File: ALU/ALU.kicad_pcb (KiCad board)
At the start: 4 copper layers, 100 x 100 mm, 73 parts, among them IC1 SN74AHCT16245ADGGR, J1 Conn_01x06_Pin, J2 Conn_02x15_Odd_Even, J3 Conn_02x15_Odd_Even, J4 Conn_02x15_Odd_Even, J5 Conn_01x01_Pin, J6 Conn_01x01_Pin, J7 Conn_01x01_Pin, J8 Conn_01x01_Pin, U1 74AHC1G08, U10 74HCT21, U11 74AHCT1G02, U12 74AHCT1G02, U13 74AHC1G08, U14 74AHC1G08, U15 74AHCT1G02, U16 74AHCT1G02, U17 74AHC1G08, U18 SN74AHC16374DGGR, U19 74AHC1G08, U2 SN74AHC16374DGGR, U20 74AHCT1G02, U21 74AHCT1G02, U3 74AHC1G04, U4 74LS181, U5 74LS181, U6 74AHC1G08, U7 74HCT11, U8 74LS181, U9 74LS181

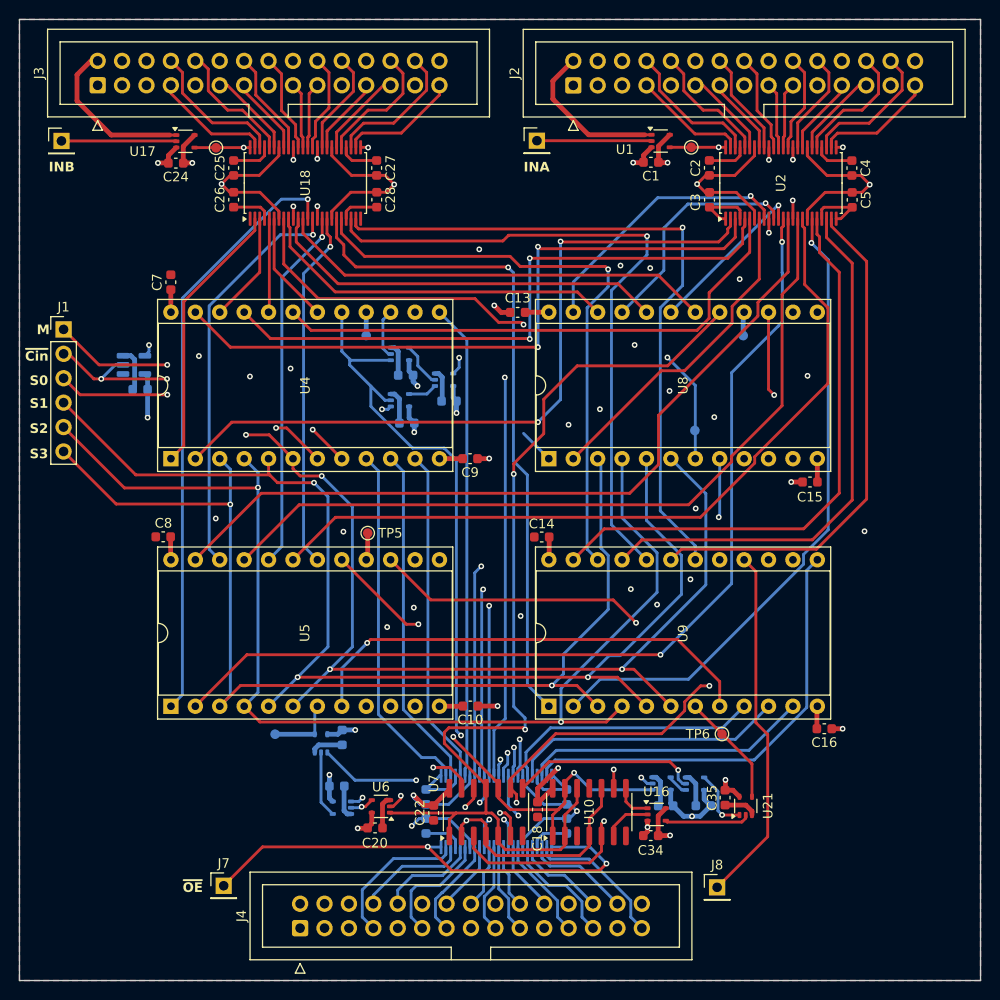
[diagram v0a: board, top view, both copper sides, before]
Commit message: Updated ALU and moved common schematics to common/ for enhanced reusability
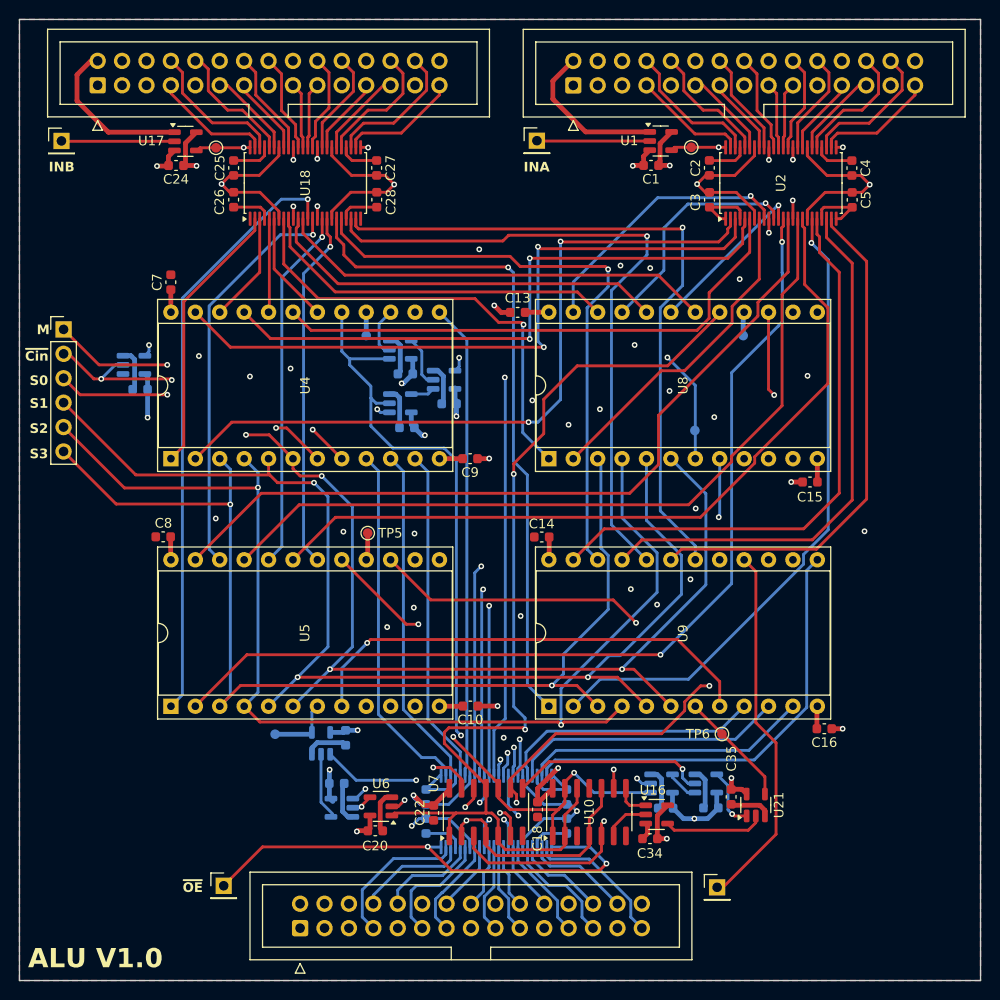
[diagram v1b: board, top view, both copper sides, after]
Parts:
- U1, U17: footprint Package_TO_SOT_SMD:SOT-353_SC-70-5 -> Package_TO_SOT_SMD:SOT-23-5
- U11, U15, U16: value 74AHCT1G02 -> 74AHC1G32DBVR; footprint Package_TO_SOT_SMD:SOT-353_SC-70-5 -> Package_TO_SOT_SMD:SOT-23-5
- U12, U20, U21: value 74AHCT1G02 -> 74AHCT1G02DBVR; footprint Package_TO_SOT_SMD:SOT-353_SC-70-5 -> Package_TO_SOT_SMD:SOT-23-5
- U13, U14, U19, U6: value 74AHC1G08 -> 74AHCT1G08DBVR; footprint Package_TO_SOT_SMD:SOT-353_SC-70-5 -> Package_TO_SOT_SMD:SOT-23-5
- moved U15 1.13 mm to (205.4, 93.5)
- moved U21 1.05 mm to (210.6, 95.7)
- moved C33 0.82 mm to (205.9, 96.0)
- moved C35 0.64 mm to (208.1, 94.9)
- moved C12 0.47 mm to (174.3, 56.5)
- moved U19 0.45 mm to (173.6, 48.4)
- moved C21 0.36 mm to (167.9, 88.7)
- moved C34 0.33 mm to (199.6, 99.2)
- moved C1 0.33 mm to (199.7, 29.2)
- moved U13 0.31 mm to (173.6, 53.9)
- moved C20 0.30 mm to (171.0, 98.4)
- moved C19 0.28 mm to (178.7, 54.0)
- moved C11 0.28 mm to (167.0, 93.5)
- moved C24 0.25 mm to (150.3, 29.2)
- moved C23 0.25 mm to (201.2, 96.1)
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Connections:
- net /alu16/carry generator/~{Cin} renamed /alu16/carry generator/Cin
- J2 pad 2: /CLK -> /bus_connector/CLK
- J3 pad 2: /CLK -> /bus_connector2/CLK
- U1 pad 1: /CLK -> /bus_connector/CLK
- U17 pad 1: /CLK -> /bus_connector2/CLK
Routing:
- net /CLK: track 33.9 -> 0.00 mm
- net /bus_connector2/CLK: track 0.00 -> 17.0 mm
- net /bus_connector/CLK: track 0.00 -> 16.4 mm
- net /INB/DOUT4: track 36.0 -> 47.4 mm
- net GND: track 139.0 -> 147.3 mm, vias 39 -> 41
- net +5V: track 171.4 -> 175.4 mm
- net Net-(U16-Pad4): track 8.87 -> 10.7 mm
- net Net-(U14-Pad4): track 2.21 -> 3.30 mm
- net /alu16/Cout: track 37.3 -> 38.4 mm
- net Net-(U19-Pad4): track 4.63 -> 5.59 mm
- net Net-(U15-Pad2): track 19.6 -> 20.6 mm
- net /INA/DOUT1: track 70.7 -> 71.6 mm
- net /alu16/carry generator/Cin: track 98.6 -> 98.0 mm
- net /S2: track 123.4 -> 124.1 mm
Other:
- board text added: "ALU V1.0"

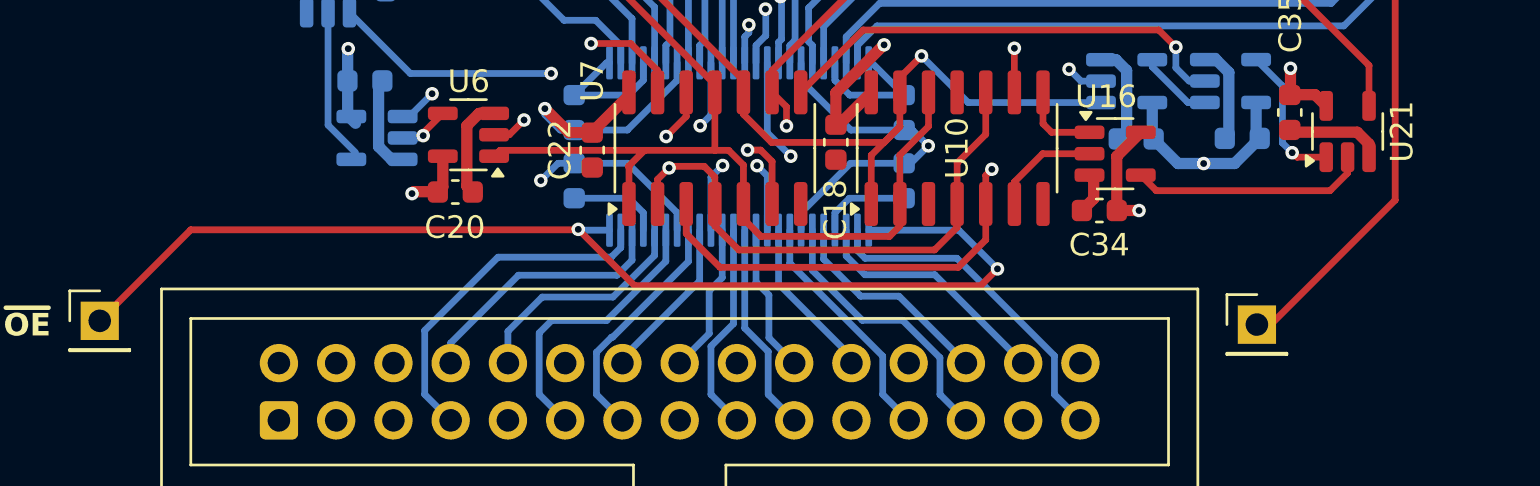
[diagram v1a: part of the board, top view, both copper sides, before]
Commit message: Fixed tri-state buffer and completed double buffer PCB
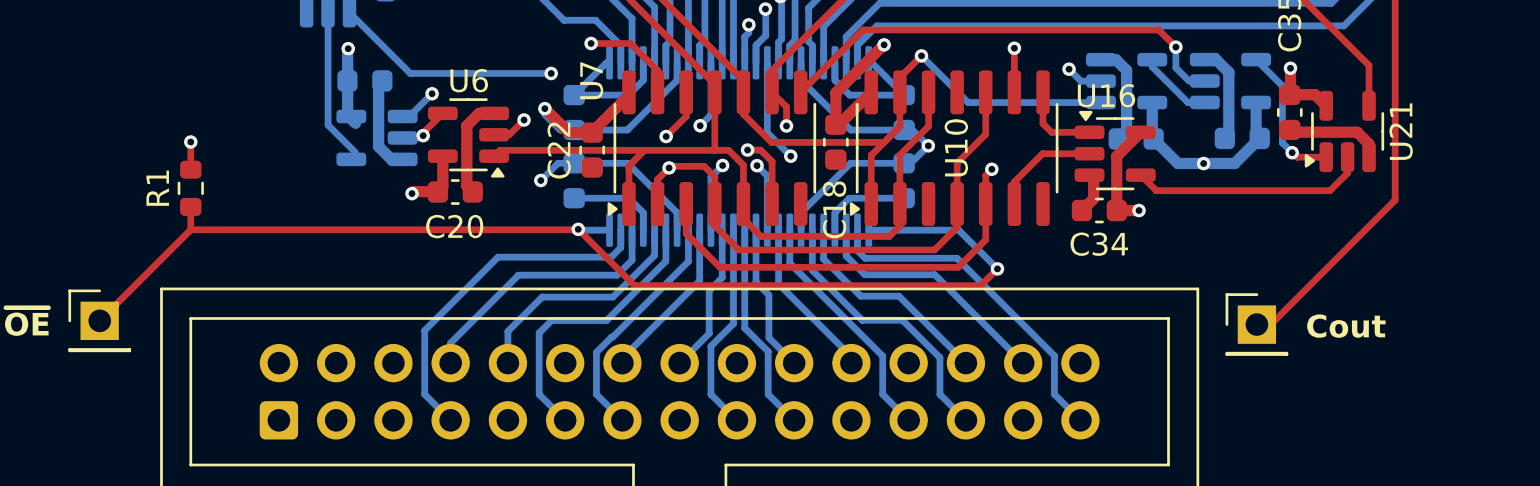
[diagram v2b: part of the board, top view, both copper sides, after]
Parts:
- added R1: 1k, Resistor_SMD:R_0603_1608Metric, F.Cu at (159.3, 98.3)
- IC1: value SN74AHCT16245ADGGR -> SN74AHCT16245DGVR
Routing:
- net +5V: track 175.4 -> 176.6 mm, vias 24 -> 25
- net /Tri-State Buf16/~{OE}: track 50.7 -> 51.7 mm
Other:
- board text added: "Cout"

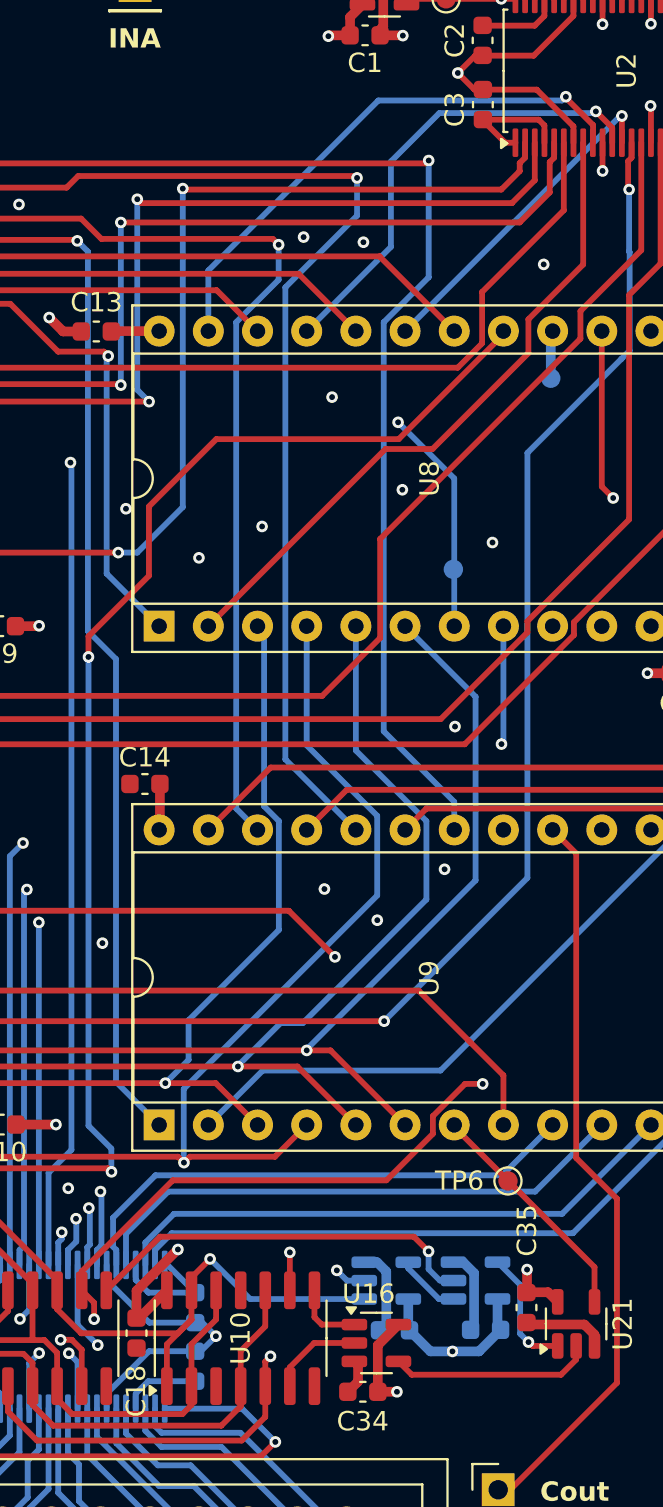
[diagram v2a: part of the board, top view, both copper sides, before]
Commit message: Fixed ERC errors
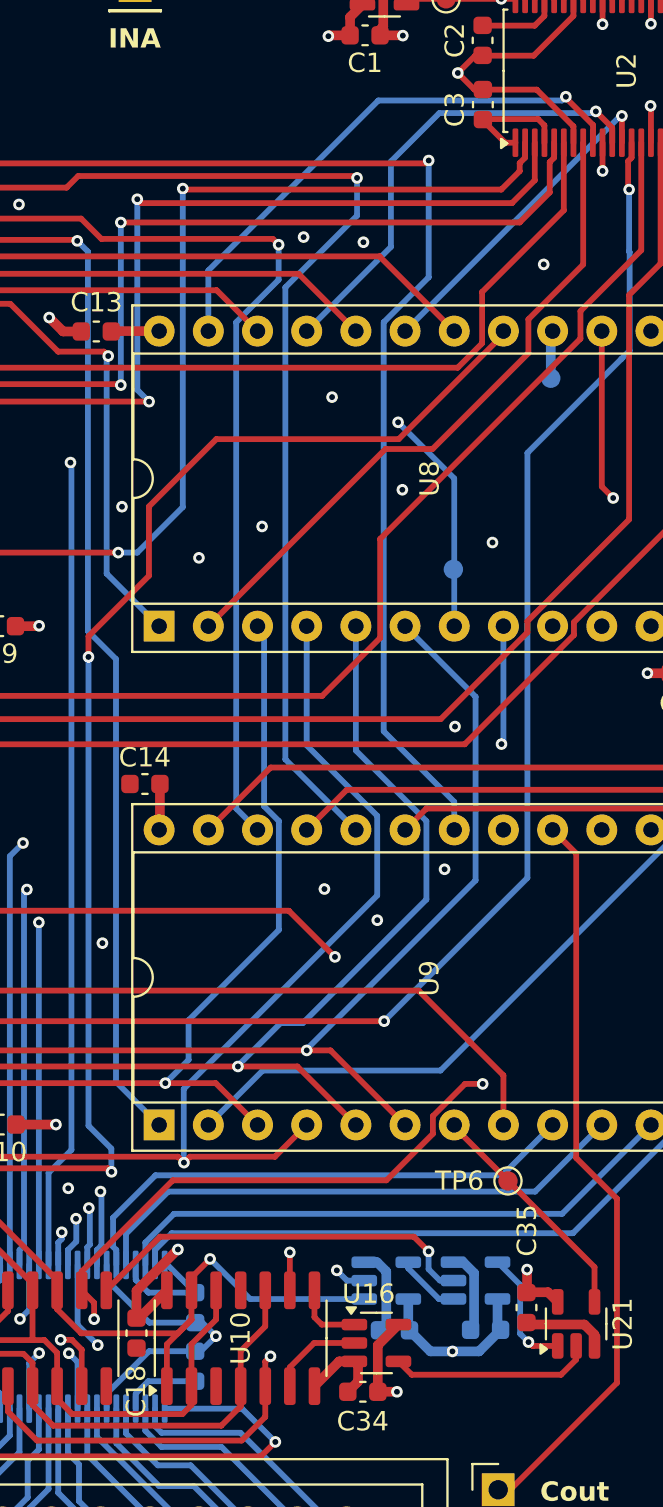
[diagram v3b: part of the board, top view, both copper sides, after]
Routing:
- net GND: track 147.3 -> 150.0 mm
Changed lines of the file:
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@@
+	)
+	(segment
+		(start 208.977 33.837)
+		(end 208.977 34.74)
+		(width 0.3)
+		(layer "F.Cu")
+		(net 1)
+	)
+	(segment
+		(start 205.734 33.51)
+		(end 208.65 33.51)
+		(width 0.3)
+		(layer "F.Cu")
+		(net 1)
 	)
 	(segment
@@
 	)
 	(segment
+		(start 208.65 33.51)
+		(end 208.977 33.837)
+		(width 0.3)
+		(layer "F.Cu")
+		(net 1)
+	)
+	(segment
 		(start 205.7641 28.685)
 		(end 208.475 28.685)
@@
 	)
 	(segment
+		(start 206.954 34.73)
+		(end 205.734 33.51)
+		(width 0.3)
+		(layer "F.Cu")
+		(net 1)
+	)
+	(segment
 		(start 162.4991 33.4509)
 		(end 162.5 33.45)
@@
 	)
 	(segment
+		(start 149.497 28.2621)
+		(end 150.1291 27.63)
+		(width 0.5)
+		(layer "F.Cu")
+		(net 1)
+	)
+	(segment
+		(start 198.38 97.67)
+		(end 197.1 98.95)
+		(width 0.5)
+		(layer "F.Cu")
+		(net 1)
+	)
+	(segment
 		(start 205.764 28.685)
 		(end 205.7641 28.685)
@@
 	)
 	(segment
-		(start 206.954 34.73)
-		(end 205.764 33.54)
-		(width 0.3)
-		(layer "F.Cu")
-		(net 1)
-	)
-	(segment
 		(start 217.02 59.7)
 		(end 217.02 62.12)
@@
 	)
 	(segment
-		(start 149.497 28.2621)
-		(end 150.1291 27.63)
-		(width 0.5)
-		(layer "F.Cu")
-		(net 1)
-	)
-	(segment
 		(start 218.9791 34.73)
 		(end 218.979 34.73)
@@
 	)
 	(segment
+		(start 199.1625 97.67)
+		(end 198.38 97.67)
+		(width 0.5)
+		(layer "F.Cu")
+		(net 1)
+	)
+	(segment
 		(start 208.977 28.1835)
 		(end 208.977 27.315)
@@
 	)
 	(segment
+		(start 171.1666 28.675)
+		(end 168.596 28.675)
+		(width 0.3)
+		(layer "F.Cu")
+		(net 1)
+	)
+	(segment
+		(start 216.97 85.51)
+		(end 217.02 85.46)
+		(width 0.5)
+		(layer "F.Cu")
+		(net 1)
+	)
+	(segment
+		(start 177.7 59.7)
+		(end 180.11 59.7)
+		(width 0.5)
+		(layer "F.Cu")
+		(net 1)
+	)
+	(segment
+		(start 217.477 34.74)
+		(end 217.477 33.768)
+		(width 0.3)
+		(layer "F.Cu")
+		(net 1)
+	)
+	(segment
+		(start 148.31 29.255)
+		(end 149.419 29.255)
+		(width 0.5)
+		(layer "F.Cu")
+		(net 1)
+	)
+	(segment
+		(start 184.12 44.48)
+		(end 183.4 43.76)
+		(width 0.5)
+		(layer "F.Cu")
+		(net 1)
+	)
+	(segment
+		(start 162.4991 27.305)
+		(end 162.4991 28.6091)
+		(width 0.3)
+		(layer "F.Cu")
+		(net 1)
+	)
+	(segment
+		(start 164.9991 34.73)
+		(end 164.9991 33.4309)
+		(width 0.3)
+		(layer "F.Cu")
+		(net 1)
+	)
+	(segment
+		(start 216.97 87.8)
+		(end 216.97 85.51)
+		(width 0.5)
+		(layer "F.Cu")
+		(net 1)
+	)
+	(segment
+		(start 199.1625 97.67)
+		(end 199.35 97.8575)
+		(width 0.5)
+		(layer "F.Cu")
+		(net 1)
+	)
+	(segment
+		(start 168.426 33.53)
+		(end 171.1766 33.53)
+		(width 0.3)
+		(layer "F.Cu")
+		(net 1)
+	)
+	(segment
+		(start 208.05 95.665)
+		(end 208.15 95.765)
+		(width 0.5)
+		(layer "F.Cu")
+		(net 1)
+	)
+	(segment
+		(start 171.167 28.675)
+		(end 171.1666 28.675)
+		(width 0.3)
+		(layer "F.Cu")
+		(net 1)
+	)
+	(segment
+		(start 167.999 28.0783)
+		(end 167.999 27.305)
+		(width 0.3)
+		(layer "F.Cu")
+		(net 1)
+	)
+	(segment
+		(start 220.654 33.54)
+		(end 219.464 34.73)
+		(width 0.3)
+		(layer "F.Cu")
+		(net 1)
+	)
+	(segment
+		(start 180.04 85.46)
+		(end 180.06 85.44)
+		(width 0.5)
+		(layer "F.Cu")
+		(net 1)
+	)
+	(segment
 		(start 207.479 34.73)
 		(end 206.954 34.73)
@@
 	)
 	(segment
-		(start 171.1666 28.675)
-		(end 168.596 28.675)
-		(width 0.3)
-		(layer "F.Cu")
-		(net 1)
-	)
-	(segment
-		(start 216.97 85.51)
-		(end 217.02 85.46)
-		(width 0.5)
-		(layer "F.Cu")
-		(net 1)
-	)
-	(segment
-		(start 208.977 33.837)
-		(end 208.977 34.74)
-		(width 0.3)
-		(layer "F.Cu")
-		(net 1)
-	)
-	(segment
-		(start 177.7 59.7)
-		(end 180.11 59.7)
-		(width 0.5)
-		(layer "F.Cu")
-		(net 1)
-	)
-	(segment
-		(start 217.477 34.74)
-		(end 217.477 33.768)
-		(width 0.3)
-		(layer "F.Cu")
-		(net 1)
-	)
-	(segment
-		(start 148.31 29.255)
-		(end 149.419 29.255)
-		(width 0.5)
-		(layer "F.Cu")
-		(net 1)
-	)
-	(segment
-		(start 184.12 44.48)
-		(end 183.4 43.76)
-		(width 0.5)
-		(layer "F.Cu")
-		(net 1)
-	)
-	(segment
-		(start 162.4991 27.305)
-		(end 162.4991 28.6091)
-		(width 0.3)
-		(layer "F.Cu")
-		(net 1)
-	)
-	(segment
-		(start 164.9991 34.73)
-		(end 164.9991 33.4309)
-		(width 0.3)
-		(layer "F.Cu")
-		(net 1)
-	)
-	(segment
-		(start 216.97 87.8)
-		(end 216.97 85.51)
-		(width 0.5)
-		(layer "F.Cu")
-		(net 1)
-	)
-	(segment
-		(start 199.1625 97.67)
-		(end 199.35 97.8575)
-		(width 0.5)
-		(layer "F.Cu")
-		(net 1)
-	)
-	(segment
-		(start 168.426 33.53)
-		(end 171.1766 33.53)
-		(width 0.3)
-		(layer "F.Cu")
-		(net 1)
-	)
-	(segment
-		(start 208.05 95.665)
-		(end 208.15 95.765)
-		(width 0.5)
-		(layer "F.Cu")
-		(net 1)
-	)
-	(segment
-		(start 171.167 28.675)
-		(end 171.1666 28.675)
-		(width 0.3)
-		(layer "F.Cu")
-		(net 1)
-	)
-	(segment
-		(start 167.999 28.0783)
-		(end 167.999 27.305)
-		(width 0.3)
-		(layer "F.Cu")
-		(net 1)
-	)
-	(segment
-		(start 220.654 33.54)
-		(end 219.464 34.73)
-		(width 0.3)
-		(layer "F.Cu")
-		(net 1)
-	)
-	(segment
-		(start 180.04 85.46)
-		(end 180.06 85.44)
-		(width 0.5)
-		(layer "F.Cu")
-		(net 1)
-	)
-	(segment
 		(start 167.999 33.9567)
 		(end 168.426 33.53)
@@
 	)
 	(segment
-		(start 208.68 33.54)
-		(end 208.977 33.837)
-		(width 0.3)
-		(layer "F.Cu")
-		(net 1)
-	)
-	(segment
 		(start 159.499 33.9567)
 		(end 159.499 34.73)
@@
 	)
 	(segment
-		(start 205.764 33.54)
-		(end 208.68 33.54)
-		(width 0.3)
-		(layer "F.Cu")
-		(net 1)
-	)
-	(segment
 		(start 217.705 33.54)
 		(end 220.654 33.54)
@@
 	)
 	(via
-		(at 187.365 53.635)
-		(size 0.6)
-		(drill 0.3)
+		(at 187.16 53.53)
+		(size 0.6)
+		(drill 0.3)
